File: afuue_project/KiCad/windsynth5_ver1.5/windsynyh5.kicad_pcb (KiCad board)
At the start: 2 copper layers, 74.9 x 99.1 mm, 35 parts, among them P1 SENSOR, P2 SPEAKER, P3 HEADPHONE, P4 EXT-POWER, P5 EXT, P6 AE-PAM8012, P7 I2C, P8 MIDI-TRS, U1 ESP32-DEVKIT-C, U2 TDA1543, U3 TDA1543

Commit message: 現状のものを一旦コミット（KORG NTS-1対応含む）
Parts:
- removed GS1, GS2: GS, Connectors:GS2
- removed U2: TDA1543, Housings_SOIC:SO-8_5.3x6.2mm_Pitch1.27mm
- removed U3: TDA1543, Housings_DIP:DIP-8_W7.62mm
- added C1: C, Pin_Headers:Pin_Header_Straight_1x02_Pitch2.54mm, F.Cu at (166.4, 144.1)
- P1, P7: moved to B.Cu
- P5: footprint Pin_Headers:Pin_Header_Straight_1x04_Pitch2.54mm -> Socket_Strips:Socket_Strip_Angled_1x04_Pitch2.54mm; moved to B.Cu
- P8: value MIDI-TRS -> TRS MIDI
- R1: moved to F.Cu
- R2, R3: value R -> 47
- moved P4 74.4 mm to (127.6, 130.8)
- moved D2 52.7 mm to (129.5, 112.4), turned to 0 degrees
- moved D4 52.7 mm to (166.4, 112.4), turned to 0 degrees
- moved D1 50.4 mm to (135.3, 114.9), turned to 180 degrees
- moved D3 50.4 mm to (140.3, 114.9), turned to 180 degrees
- moved P6 48.1 mm to (134.0, 97.2), turned to 0 degrees
- moved P1 48.1 mm to (161.9, 124.5)
- moved P2 36.2 mm to (132.7, 106.0), turned to 90 degrees
- moved P5 35.5 mm to (129.5, 69.2), turned to 270 degrees
- moved P7 11.6 mm to (163.2, 119.4), turned to 90 degrees
- moved R1 1.42 mm to (151.1, 148.0), turned to 90 degrees
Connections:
- D5 pad 2: +3V3 -> Net-(D5-Pad2)
- P1 pad 1: +3V3 -> Net-(D5-Pad2)
- P4 pad 2: Net-(P4-Pad2) -> Net-(D5-Pad2)
- P5 pad 3: Net-(P5-Pad3) -> Net-(D1-Pad2)
- P7 pad 2: +3V3 -> Net-(D5-Pad2)
- R1 pad 1: Net-(GS1-Pad2) -> Net-(R1-Pad1)
- R2 pad 1: +3V3 -> Net-(D5-Pad2)
- U1 pad 1: +3V3 -> Net-(D5-Pad2)
- U1 pad 17: Net-(D1-Pad2) -> (no net)
- U1 pad 18: Net-(P4-Pad2) -> (no net)
- U1 pad 25: Net-(P5-Pad2) -> (no net)
- U1 pad 26: Net-(P5-Pad3) -> Net-(KeyUP1-Pad1)
- U1 pad 34: Net-(KeyUP1-Pad1) -> (no net)
- U1 pad 5: Net-(U1-Pad5) -> (no net)
- U1 pad 6: Net-(U1-Pad6) -> (no net)
- U1 pad 7: Net-(U1-Pad7) -> Net-(P5-Pad2)
- U1 pad 8: (no net) -> Net-(D1-Pad2)
- U1 pad 9: Net-(GS1-Pad1) -> Net-(R1-Pad1)
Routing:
- net +3V3: track 159.9 -> 0.00 mm, vias 7 -> 0
- net +5V: track 102.2 -> 25.3 mm, vias 3 -> 2
- net Net-(D5-Pad2): track 0.00 -> 73.2 mm, vias 0 -> 3
- net Net-(KeyUP1-Pad1): track 71.5 -> 0.00 mm, vias 2 -> 0
- net Net-(R1-Pad1): track 0.00 -> 70.1 mm
- net Net-(GS1-Pad2): track 55.7 -> 0.00 mm
- net Net-(P1-Pad3): track 82.4 -> 31.8 mm, vias 2 -> 0
- net Net-(KeyDown1-Pad1): track 50.1 -> 0.63 mm, vias 2 -> 0
- net Net-(P3-Pad2): track 81.3 -> 34.5 mm
- net Net-(P1-Pad4): track 85.3 -> 42.0 mm, vias 2 -> 0
- net Net-(D1-Pad2): track 10.2 -> 52.4 mm, vias 0 -> 1
- net Net-(GS1-Pad1): track 36.4 -> 0.00 mm
- net Net-(R3-Pad1): track 0.00 -> 35.7 mm
- net GND: track 483.0 -> 453.0 mm, vias 1 -> 0
- net Net-(KeyB1-Pad1): track 96.4 -> 68.8 mm, vias 2 -> 0
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
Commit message: 基板発注したので
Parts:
- removed D2, D4, D6: Led_Small, Pin_Headers:Pin_Header_Straight_1x02_Pitch2.54mm
- removed D3, D5: D, Pin_Headers:Pin_Header_Straight_1x02_Pitch2.54mm
- removed P1: SENSOR, Socket_Strips:Socket_Strip_Angled_1x04_Pitch2.54mm
- removed P2: SPEAKER, Pin_Headers:Pin_Header_Straight_1x02_Pitch2.54mm
- removed P4: EXT-POWER, Socket_Strips:Socket_Strip_Straight_1x03_Pitch2.54mm
- removed P7: I2C, Pin_Headers:Pin_Header_Straight_1x05_Pitch2.54mm
- added EXT-POWER: EXT-POWER, Socket_Strips:Socket_Strip_Straight_1x03_Pitch2.00mm, B.Cu at (131.4, 109.2)
- added I2C: I2C, Pin_Headers:Pin_Header_Straight_1x05_Pitch2.00mm, F.Cu at (164.5, 149.9)
- added SENSOR: SENSOR, Socket_Strips:Socket_Strip_Angled_1x04_Pitch2.00mm, B.Cu at (159.4, 137.8)
- added SPEAKER: SPEAKER, UGSM30:USGM30, F.Cu at (153.0, 119.4)
- D1: value D -> Led_Small
- moved C1 36.7 mm to (130.2, 137.8)
- moved VOLUME 36.3 mm to (126.4, 157.5)
- moved D1 25.6 mm to (148.0, 92.7)
- moved R1 21.3 mm to (130.2, 144.1), turned to 0 degrees
- renumbered P6 to AE-PAM8012, U1 to ESP32-DEVKIT-C, P5 to EXT, P3 to HEADPHONE, KeyA1 to KeyA, KeyB1 to KeyB, KeyD1 to KeyD, KeyDown1 to KeyDown, KeyE1 to KeyE, KeyEb1 to KeyEb, KeyF1 to KeyF, KeyG1 to KeyG, KeyG#1 to KeyG#, KeyLowC1 to KeyLowC, KeyLowC#1 to KeyLowC#, KeyUP1 to KeyUP, P8 to TRS-MIDI, RV1 to VOLUME
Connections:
- D1 pad 1: Net-(D1-Pad1) -> GND
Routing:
- net +5V: track 25.3 -> 214.5 mm
- net Net-(KeyUP1-Pad1): track 0.00 -> 93.1 mm, vias 0 -> 4
- net Net-(KeyDown1-Pad1): track 0.63 -> 54.0 mm, vias 0 -> 3
- net Net-(P2-Pad1): track 7.25 -> 45.8 mm, vias 0 -> 2
- net Net-(P1-Pad1): track 73.2 -> 110.7 mm, vias 3 -> 5
- net Net-(P2-Pad2): track 7.25 -> 37.0 mm, vias 0 -> 2
- net Net-(P1-Pad3): track 31.8 -> 61.0 mm
- net Net-(P1-Pad4): track 42.0 -> 70.8 mm
- net Net-(D1-Pad2): track 52.4 -> 33.7 mm, vias 1 -> 2
- net Net-(R1-Pad1): track 70.1 -> 85.4 mm
- net GND: track 453.0 -> 466.5 mm
- net Net-(P3-Pad3): track 111.7 -> 118.9 mm, vias 2 -> 0
- net Net-(C1-Pad1): track 15.6 -> 21.9 mm
- net Net-(D1-Pad1): track 5.72 -> 0.00 mm
- net Net-(D5-Pad1): track 5.08 -> 0.00 mm
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- added copper zone on B.Cu, net GND
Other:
- board size 74.9 x 99.1 mm -> 74.9 x 101.6 mm
- board text added: "AFUUE BOARD VER1.5 - 20/11/03 @OtooneDev"
- board text removed: "AFUUE BOARD VER1.5 20/08/03 OtooneDev"
- board text removed: "SPEAKER"

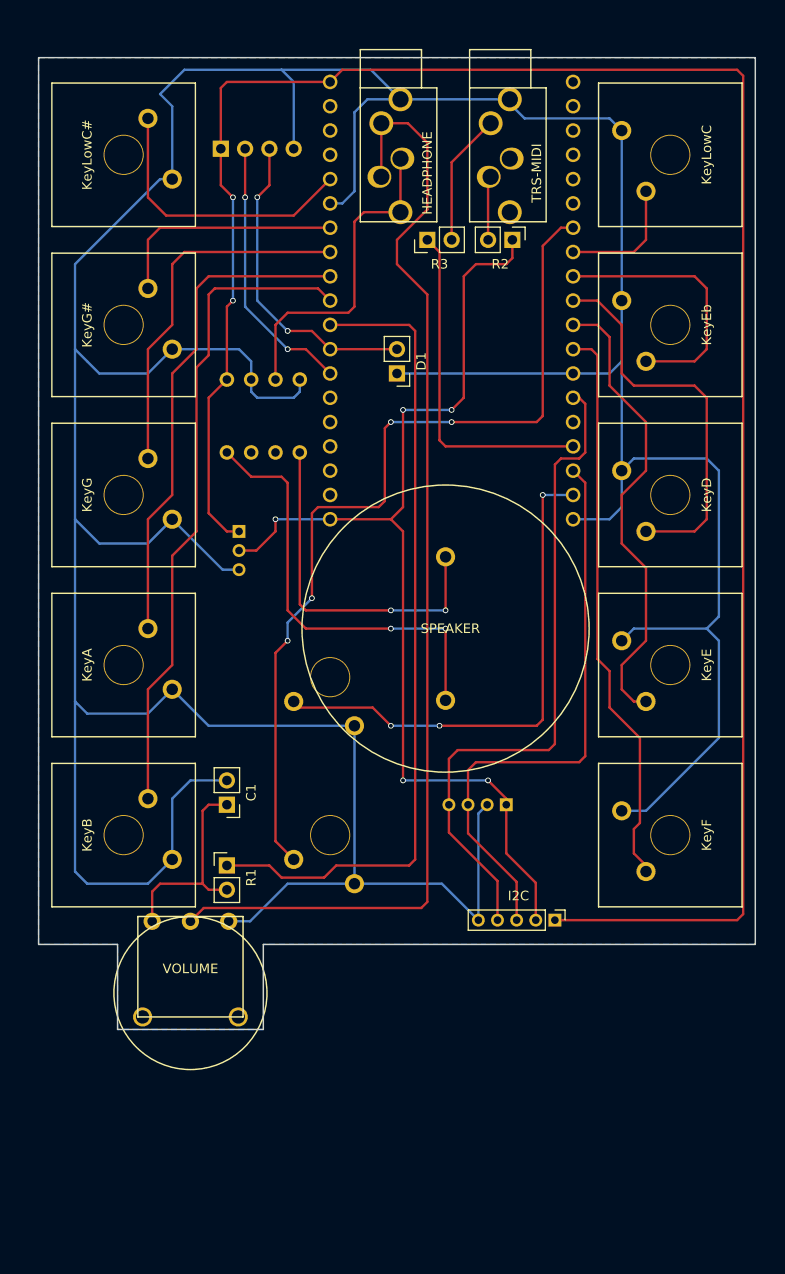
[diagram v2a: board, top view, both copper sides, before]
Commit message: 電池内蔵版v06のソースやデータを追加
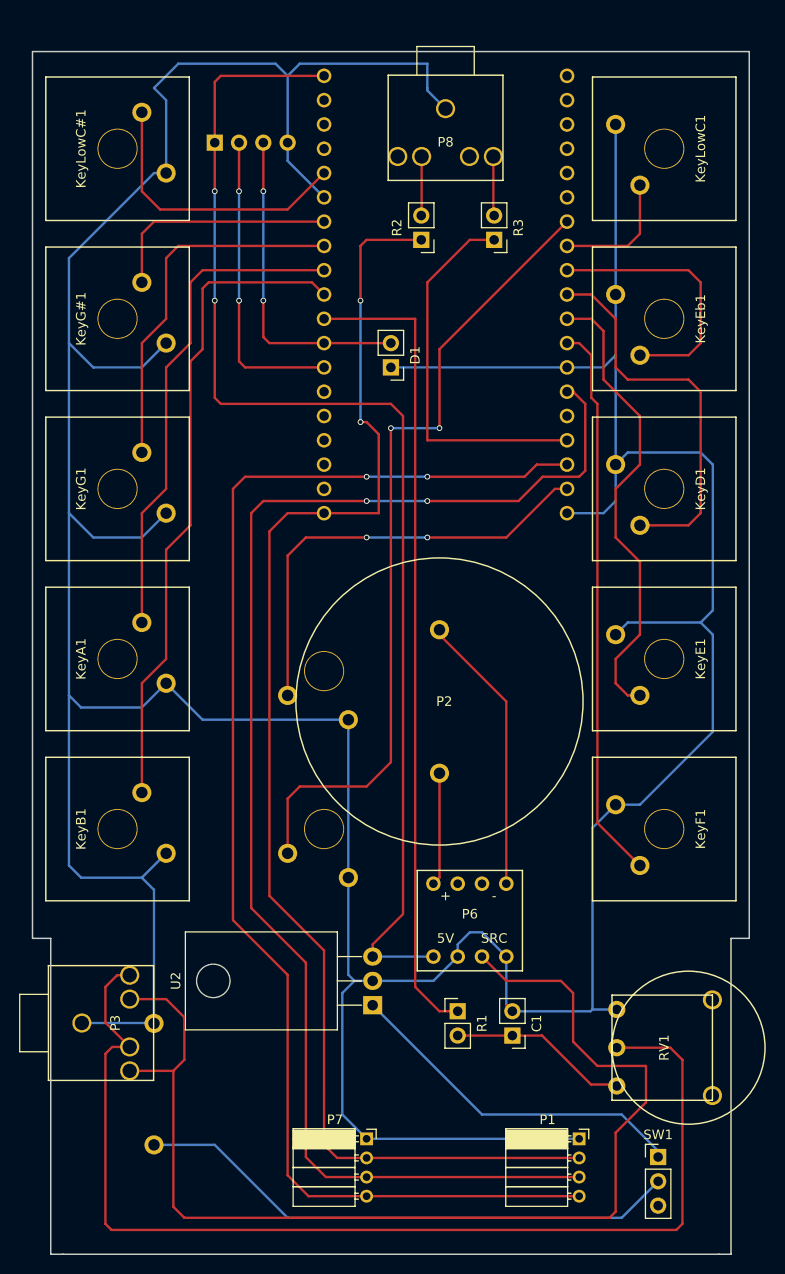
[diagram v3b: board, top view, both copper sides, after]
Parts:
- removed AE-PAM8012: AE-PAM8012, AE-PAM8012:AE-PAM8012
- removed ESP32-DEVKIT-C: ESP32-DEVKIT-C, esp32-devkit-c:ESP32-DEVKIT-C
- removed EXT: EXT, Socket_Strips:Socket_Strip_Angled_1x04_Pitch2.54mm
- removed EXT-POWER: EXT-POWER, Socket_Strips:Socket_Strip_Straight_1x03_Pitch2.00mm
- removed HEADPHONE: HEADPHONE, PJ325:PJ325
- removed I2C: I2C, Pin_Headers:Pin_Header_Straight_1x05_Pitch2.00mm
- removed KeyA: KeyA, CherryMX-Switch:CherryMX-Switch
- removed KeyB: KeyB, CherryMX-Switch:CherryMX-Switch
- removed KeyD: KeyD, CherryMX-Switch:CherryMX-Switch
- removed KeyDown: KeyDown, CherryMX-Switch:CherryMX-Switch
- removed KeyE: KeyE, CherryMX-Switch:CherryMX-Switch
- removed KeyEb: KeyEb, CherryMX-Switch:CherryMX-Switch
- removed KeyF: KeyF, CherryMX-Switch:CherryMX-Switch
- removed KeyG: KeyG, CherryMX-Switch:CherryMX-Switch
- removed KeyG#: KeyG#, CherryMX-Switch:CherryMX-Switch
- removed KeyLowC: KeyLowC, CherryMX-Switch:CherryMX-Switch
- removed KeyLowC#: KeyLowC#, CherryMX-Switch:CherryMX-Switch
- removed KeyUP: KeyUp, CherryMX-Switch:CherryMX-Switch
- removed SENSOR: SENSOR, Socket_Strips:Socket_Strip_Angled_1x04_Pitch2.00mm
- removed SPEAKER: SPEAKER, UGSM30:USGM30
- removed TRS-MIDI: TRS MIDI, PJ325:PJ325
- removed VOLUME: POT, R1001-N16:R1001-N16
- added KeyA1: KeyA, CherryMX-Switch:CherryMX-Switch, F.Cu at (118.7, 122.6)
- added KeyB1: KeyB, CherryMX-Switch:CherryMX-Switch, F.Cu at (118.7, 140.3)
- added KeyD1: KeyD, CherryMX-Switch:CherryMX-Switch, F.Cu at (175.9, 104.8)
- added KeyDown1: KeyDown, CherryMX-Switch:CherryMX-Switch, B.Cu at (140.3, 123.8)
- added KeyE1: KeyE, CherryMX-Switch:CherryMX-Switch, F.Cu at (175.9, 122.6)
- added KeyEb1: KeyEb, CherryMX-Switch:CherryMX-Switch, F.Cu at (175.9, 87.0)
- added KeyF1: KeyF, CherryMX-Switch:CherryMX-Switch, F.Cu at (175.9, 140.3)
- added KeyG#1: KeyG#, CherryMX-Switch:CherryMX-Switch, F.Cu at (118.7, 87.0)
- added KeyG1: KeyG, CherryMX-Switch:CherryMX-Switch, F.Cu at (118.7, 104.8)
- added KeyLowC#1: KeyLowC#, CherryMX-Switch:CherryMX-Switch, F.Cu at (118.7, 69.2)
- added KeyLowC1: KeyLowC, CherryMX-Switch:CherryMX-Switch, F.Cu at (175.9, 69.2)
- added KeyUP1: KeyUp, CherryMX-Switch:CherryMX-Switch, B.Cu at (140.3, 140.3)
- added P1: SENSOR, Socket_Strips:Socket_Strip_Angled_1x04_Pitch2.00mm, F.Cu at (167.0, 172.7)
- added P2: SPEAKER, UGSM30:USGM30, F.Cu at (152.4, 127.0)
- added P3: HEADPHONE, HPJack_PJ307:PJ-307 AudioJack, F.Cu at (123.0, 160.6)
- added P4: POWER, BH-9V-3P24:BH-9V-3P24, B.Cu at (122.6, 167.0)
- added P5: EXT, Socket_Strips:Socket_Strip_Angled_1x04_Pitch2.54mm, B.Cu at (128.9, 68.6)
- added P6: AE-PAM8012, AE-PAM8012:AE-PAM8012, F.Cu at (155.6, 149.9)
- added P7: I2C, Socket_Strips:Socket_Strip_Angled_1x04_Pitch2.00mm, F.Cu at (144.8, 172.7)
- added P8: TRS MIDI, HPJack_PJ307:PJ-307 AudioJack, F.Cu at (153.0, 73.0)
- added RV1: POT, R1001-N16:R1001-N16, F.Cu at (178.4, 163.2)
- added SW1: SW_SPDT, Connector_PinHeader_2.54mm:PinHeader_1x03_P2.54mm_Vertical, F.Cu at (175.3, 174.6)
- added U1: ESP32-DEVKIT-C, esp32-devkit-c:ESP32-DEVKIT-C, B.Cu at (153.0, 84.5)
- added U2: L7805, Package_TO_SOT_THT:TO-220-3_Horizontal_TabDown, F.Cu at (145.4, 158.8)
- moved C1 38.4 mm to (160.0, 161.9)
- moved R1 28.5 mm to (154.3, 159.4)
- moved R2 9.53 mm to (150.5, 78.7), turned to 180 degrees
- moved R3 6.99 mm to (158.1, 78.7), turned to 180 degrees
- moved D1 0.90 mm to (147.3, 92.1)
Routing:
- net Net-(P3-Pad2): track 34.5 -> 119.7 mm
- net Net-(P1-Pad3): track 61.0 -> 145.9 mm, vias 0 -> 2
- net +5V: track 214.5 -> 130.0 mm
- net Net-(P1-Pad4): track 70.8 -> 141.5 mm, vias 0 -> 2
- net Net-(P4-Pad1): track 0.00 -> 57.4 mm
- net +9V: track 0.00 -> 36.8 mm
- net Net-(P2-Pad1): track 45.8 -> 11.8 mm, vias 2 -> 0
- net Net-(P1-Pad2): track 110.7 -> 141.7 mm, vias 5 -> 2
- net GND: track 466.5 -> 490.8 mm
- net Net-(KeyUP1-Pad1): track 93.1 -> 85.2 mm, vias 4 -> 2
- net Net-(P8-Pad5): track 13.9 -> 6.21 mm
- net Net-(P2-Pad2): track 37.0 -> 29.4 mm, vias 2 -> 0
- net Net-(KeyDown1-Pad1): track 54.0 -> 46.7 mm, vias 3 -> 2
- net Net-(R3-Pad1): track 35.7 -> 39.9 mm
- net Net-(P5-Pad2): track 29.6 -> 33.3 mm
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- removed copper zone on B.Cu, net GND
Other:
- board size 74.9 x 101.6 mm -> 74.9 x 125.7 mm
- board text added: "AFUUE BOARD VER1.6 - 20/12/26 @OtooneDev"
- board text removed: "AFUUE BOARD VER1.5 - 20/11/03 @OtooneDev"
